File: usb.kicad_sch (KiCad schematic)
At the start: 15 parts, among them J4 CONN_02X03, U1 LFE5U-25F-6BG381C, U6 FT231XQ

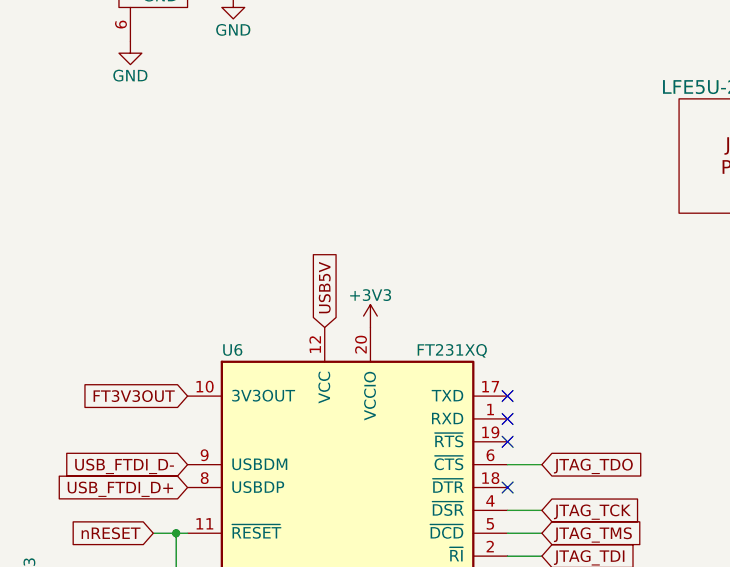
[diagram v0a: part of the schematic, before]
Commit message: Routed Level Shifters + Flash
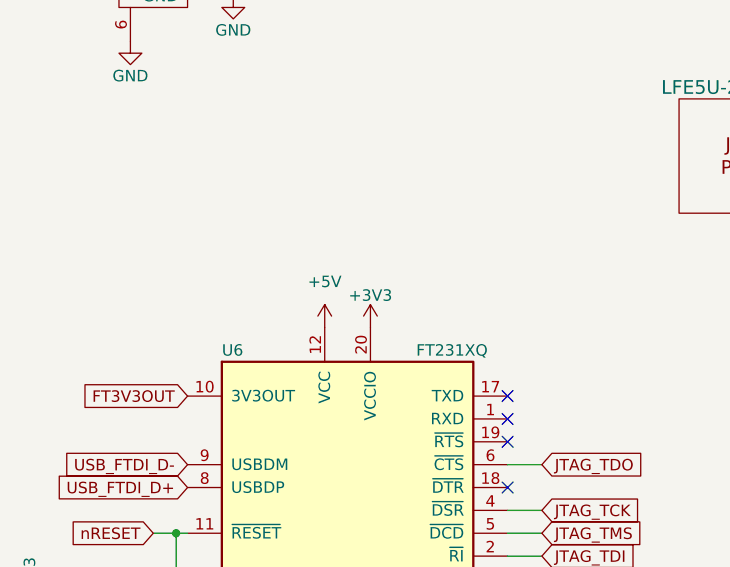
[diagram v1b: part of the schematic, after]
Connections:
- net USB5V: no longer U6.12 (VCC)
- new net +5V: U6.12 (VCC)
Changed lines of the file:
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@@
 		)
 	)
-	(global_label "USB5V"
-		(shape input)
-		(at 64.77 77.47 90)
-		(effects
-			(font
-				(size 1.27 1.27)
-			)
-			(justify left)
-		)
-		(property "Intersheetrefs" "${INTERSHEET_REFS}"
-			(at 64.77 77.47 0)
-			(effects
-				(font
-					(size 1.27 1.27)
-				)
-				(hide yes)
-			)
-		)
-	)
 	(global_label "FTDI_nTXLED"
 		(shape input)
@@
 					(unit 1)
 				)
+			)
+		)
+	)
+	(symbol
+		(lib_id "power:+5V")
+		(at 64.77 77.47 0)
+		(unit 1)
+		(exclude_from_sim no)
+		(in_bom yes)
+		(on_board yes)
+		(dnp no)
+		(fields_autoplaced yes)
+		(property "Reference" "#PWR063"
+			(at 64.77 81.28 0)
+			(effects
+				(font
+					(size 1.27 1.27)
+				)
+				(hide yes)
+			)
+		)
+		(property "Value" "+5V"
+			(at 64.77 72.39 0)
+			(effects
+				(font
+					(size 1.27 1.27)
+				)
+			)
+		)
+		(property "Footprint" ""
+			(at 64.77 77.47 0)
+			(effects
+				(font
+					(size 1.27 1.27)
+				)
+				(hide yes)
+			)
+		)
+		(property "Datasheet" ""
+			(at 64.77 77.47 0)
+			(effects
+				(font
+					(size 1.27 1.27)
+				)
+				(hide yes)
+			)
+		)
+		(property "Description" "Power symbol creates a global label with name \"+5V\""
+			(at 64.77 77.47 0)
+			(effects
+				(font
+					(size 1.27 1.27)
+				)
+				(hide yes)
+			)
+		)
+		(pin "1"
+		)
+		(instances
+			(project ""
+				(path "/d1b325fc-ebad-476a-a3a3-dff47a9f73d8/f5fc8b61-abb6-4157-b906-4734563f1ca7"
+					(reference "#PWR063")
+					(unit 1)
+				)
